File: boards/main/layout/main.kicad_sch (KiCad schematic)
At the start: 150 parts, among them IC1 STM32H725RGV6, IC2 LSM6DSVTR, IC3 TSC2020IYST, IC4 TSC2020IYST, IC5 L6205D013TR, IC6 STSPIN958TR, IC7 L6981N33DR, J1 B02B-PASK(LF)(SN), M1 B02B-PASK(LF)(SN), M2 B02B-PASK(LF)(SN), M3 B02B-PASK(LF)(SN), P1 PZ254V-11-04P, Q1 AO3400A, Q2 AO3400A, Q3 AO3400A, Q4 AO3400A, Q5 AO3400A, Q6 HSBB3072, SW1 DSHP04TJGER, SW2 GT-TC048B-H025-L1, SW3 GT-TC048B-H025-L1, SW4 MK-12D18-G040, SW5 GT-TC048B-H025-L1, U1 TPS611781RNWR, U2 GT-USB-7010ASV, U3 CJA1117B-3.3

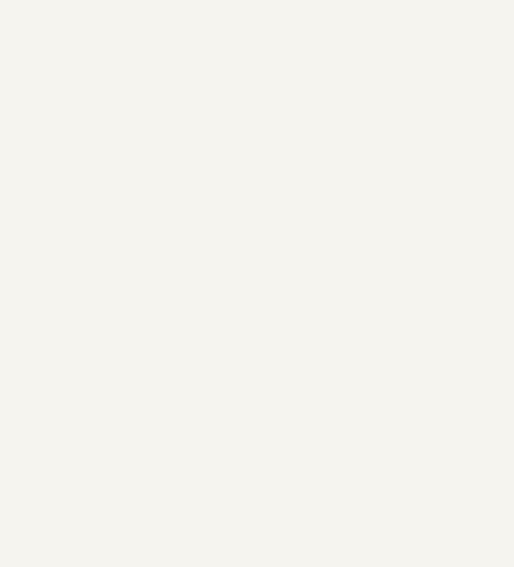
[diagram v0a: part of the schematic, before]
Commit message: ✨ Add the M2 screw holes to the main board
The previous board's four screw holes were footprints without a designator. They are now
H1-H4, instances of a new micras/MountingHole package (2.4 mm NPTH, the previous footprint),
declared in changes.toml as added parts.
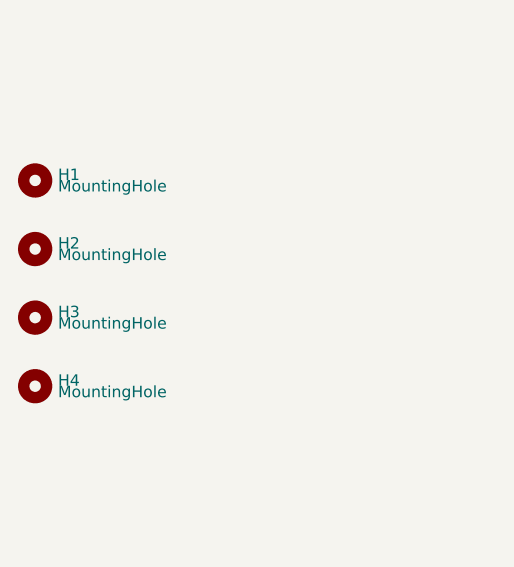
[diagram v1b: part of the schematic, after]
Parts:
- added H1, H2, H3, H4: MountingHole, Team-Micras_MicrasPCB_components_micras_MountingHole:MountingHole_2.4mm_NPTH, symbol MountingHole

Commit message: 🚚 Transfer the Altium pour, teardrop and outline settings to the layouts
The transfer scripts now carry what KiCad's Altium importer drops, and
the layouts are regenerated with them:

- Teardrops (converted to plain zones) fill with a 0.1 mm minimum width
  instead of the importer's 0.25 mm, which left 652 of 786 (main), 5 of
  25 (encoder) and 10 of 46 (bluetooth) teardrops without copper. 0.1 mm
  is JLCPCB's minimum copper feature: 0.0254 mm fills slightly more but
  fails the DFM feature width on all three boards.
- Pours use the Altium polygons' neck width as minimum width (0.1 mm;
  0.4 mm on the encoder's bottom pour, which keeps it out of the channels
  between the SPI tracks, 0.3 mm on the bluetooth plug pour).
- Inner-layer pours relieve through-hole pads (0.254 mm spokes and gap,
  Altium rule PolygonConnect); outer pours stay solid.
- Main In1/In2 keep Altium's 1.559 / 2.074 mm voids around H1-H4
  (copper-pour keepouts).
- Edge.Cuts lines under 1 um (main 6, encoder 1, bluetooth 7) are left
  out and their neighbours joined, so KiCad reads the outlines as valid.
- The board mask expansion is copied from the previous board (0.02 mm);
  main takes the spec's aux origin.
- D4/D5 and bluetooth D1 3D models are scaled to the datasheet heights.
- rework.py catches all six teardrops of the removed C1 VBAT chain (three
  were left as stubs, invisible while unfilled).
- The encoder drops an embedded TSSOP-14 STEP no footprint uses; the
  bluetooth script calls previous.altium_pcb (renamed).

The main layout footprints were resynced from their packages
(pcb layout --sync-footprints), which brings the new WallSensor
silkscreen, R31-R33 and U2's keepouts on all four copper layers.
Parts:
- R31, R32, R33: footprint stdlib_kicad-footprints_Resistor_SMD:R_2512_6332Metric -> Team-Micras_MicrasPCB_components_micras_R2512:RESC6432X89N; symbol R_Small -> R2512
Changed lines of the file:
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@@
 	)
 	(symbol
-		(lib_id "R_Small")
+		(lib_id "R2512")
 		(at 1300.48 736.6 0)
 		(unit 1)
@@
 			)
 		)
-		(property "Footprint" "stdlib_kicad-footprints_Resistor_SMD:R_2512_6332Metric"
+		(property "Footprint" "Team-Micras_MicrasPCB_components_micras_R2512:RESC6432X89N"
 			(at 1300.48 736.6 0)
 			(hide yes)
@@
 	)
 	(symbol
-		(lib_id "R_Small")
+		(lib_id "R2512")
 		(at 1249.68 679.45 0)
 		(unit 1)
@@
 			)
 		)
-		(property "Footprint" "stdlib_kicad-footprints_Resistor_SMD:R_2512_6332Metric"
+		(property "Footprint" "Team-Micras_MicrasPCB_components_micras_R2512:RESC6432X89N"
 			(at 1249.68 679.45 0)
 			(hide yes)
@@
 	)
 	(symbol
-		(lib_id "R_Small")
+		(lib_id "R2512")
 		(at 1270 679.45 0)
 		(unit 1)
@@
 			)
 		)
-		(property "Footprint" "stdlib_kicad-footprints_Resistor_SMD:R_2512_6332Metric"
+		(property "Footprint" "Team-Micras_MicrasPCB_components_micras_R2512:RESC6432X89N"
 			(at 1270 679.45 0)
 			(hide yes)

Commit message: ✨ Give each main-board module its own schematic sheet
Regulators, Drivers, Sensors and Peripherals declare Project(path="layout", layout=False), so pcb apply writes them as sheets of layout/main.kicad_sch (REGULATORS, DRIVERS, SENSORS, PERIPHERALS.kicad_sch) and the layout stays the board's: main.kicad_pcb is byte-identical.

make gen deletes every .kicad_sch of a layout before pcb apply: pcb refuses to write a new root over existing module sheets, and a regenerated sheet must not keep labels from an older generator.

ERC fails on the sheets until the ports take their nets' names (next commit) and the warnings pcb 0.4.81 leaves on module sheets are accepted (diodeinc/pcb#1520).
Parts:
- removed BZ1: FUET-5030, Team-Micras_MicrasPCB_components_fuet_FUET-5030:BUZ-SMD_FST-5030, symbol FUET-5030
- removed C18, C19, C20, C21, C24, C25, C32, C38, C55, C60: 100nF 10% 50V X7R, stdlib_kicad-footprints_Capacitor_SMD:C_0402_1005Metric, symbol C_Small
- removed C22, C23: 18pF 5% 50V C0G, stdlib_kicad-footprints_Capacitor_SMD:C_0402_1005Metric, symbol C_Small
- removed C26, C27, C28, C29, C33, C53, C54: 1uF 10% 25V X5R, stdlib_kicad-footprints_Capacitor_SMD:C_0402_1005Metric, symbol C_Small
- removed C30, C40, C41: 10nF 10% 50V X7R, stdlib_kicad-footprints_Capacitor_SMD:C_0402_1005Metric, symbol C_Small
- removed C31: 220nF 10% 16V X7R, stdlib_kicad-footprints_Capacitor_SMD:C_0402_1005Metric, symbol C_Small
- removed C34, C35: 470nF 10% 25V X7R, stdlib_kicad-footprints_Capacitor_SMD:C_0603_1608Metric, symbol C_Small
- removed C36: 220uF 20% 16V, Team-Micras_MicrasPCB_components_acmecon_VT1C221M0605:CAP-SMD_BD6.3-L6.6-W6.6-LS7.3-FD, symbol VT1C221M0605
- removed C37: 100uF 20% 25V, Team-Micras_MicrasPCB_components_jierr_JVS25V100M6X4:CAP-SMD_BD6.3-L6.6-W6.6-LS7.3-FD_JVS25V100M6X4, symbol JVS25V100M6X4
- removed C39: 220nF 10% 50V X7R, stdlib_kicad-footprints_Capacitor_SMD:C_0805_2012Metric, symbol C_Small
- removed C42: 470pF 10% 50V X7R, stdlib_kicad-footprints_Capacitor_SMD:C_0402_1005Metric, symbol C_Small
- removed C43: 220nF 10% 25V X7R, stdlib_kicad-footprints_Capacitor_SMD:C_0603_1608Metric, symbol C_Small
- removed C44, C45: 10uF 10% 50V X5R, stdlib_kicad-footprints_Capacitor_SMD:C_0805_2012Metric, symbol C_Small
- removed C46, C47: 22uF 20% 35V X5R, stdlib_kicad-footprints_Capacitor_SMD:C_0805_2012Metric, symbol C_Small
- removed C48: 4.7uF 10% 25V X5R, stdlib_kicad-footprints_Capacitor_SMD:C_0805_2012Metric, symbol C_Small
- removed C49, C50, C51, C57: 22uF 20% 25V X5R, stdlib_kicad-footprints_Capacitor_SMD:C_0805_2012Metric, symbol C_Small
- removed C52: 10uF 20% 25V X5R, stdlib_kicad-footprints_Capacitor_SMD:C_0603_1608Metric, symbol C_Small
- removed C56: 220uF 20% 6.3V X5R, stdlib_kicad-footprints_Capacitor_SMD:C_1206_3216Metric, symbol C_Small
- removed D1, D2: WS2815C-2020-4P, Team-Micras_MicrasPCB_components_worldsemi_WS2815C-2020:LED-SMD_4P-L2.2-W2.0-P1.00_WS2815C-2020-4P, symbol WS2815C-2020-4P
- removed D3, D6, D7: 1N4148W, Team-Micras_MicrasPCB_components_hongjiacheng_1N4148W:SOD-123_L2.7-W1.6-LS3.7-FD, symbol 1N4148W
- removed D4: LED YELLOW, stdlib_kicad-footprints_LED_SMD:LED_0603_1608Metric, symbol LED_Small_Filled_Yellow
- removed D5: LED RED, stdlib_kicad-footprints_LED_SMD:LED_0603_1608Metric, symbol LED_Small_Filled_Red
- removed EC1, EC2: EncoderSlot, Team-Micras_MicrasPCB_components_micras_EncoderSlot:EncoderSlot_2x4_P0.95mm, symbol EncoderSlot
- removed F1: KASML010, Team-Micras_MicrasPCB_components_kuu_KASML010:Fuse_0402, symbol KASML010
- removed IC2: LSM6DSVTR, Team-Micras_MicrasPCB_components_st_LSM6DSV:LGA-14_3x2.5mm_P0.5mm, symbol LSM6DSV
- removed IC3, IC4: TSC2020IYST, Team-Micras_MicrasPCB_components_st_TSC2020:SOP65P490X110-8N, symbol TSC2020
- removed IC5: L6205D013TR, Team-Micras_MicrasPCB_components_st_L6205D:SOIC127P1032X265-20N, symbol L6205D
- removed IC6: STSPIN958TR, Team-Micras_MicrasPCB_components_st_STSPIN958:QFN50P500X500X100-33N-D, symbol STSPIN958
- removed IC7: L6981N33DR, Team-Micras_MicrasPCB_components_st_L6981:SOIC127P600X175-8N, symbol L6981N33DR
- removed J1, M1, M2, M3: B02B-PASK(LF)(SN), Team-Micras_MicrasPCB_components_jst_B02B-PASK:JST_PA_B02B-PASK_1x02_P2.00mm_Vertical, symbol B02B-PASK
- removed L2: 1uH 20% 23A, Team-Micras_MicrasPCB_components_coilcraft_XAL6030-102:XAL6030, symbol XAL6030-102MEB
- removed L3: 22uH 20% 2.8A, Team-Micras_MicrasPCB_components_yjycoin_YSPIA0645-220M:IND-SMD_L6.5-W6.0, symbol YSPIA0645-220M
- removed Q1, Q2, Q3, Q4, Q5: AO3400A, Team-Micras_MicrasPCB_components_aos_AO3400A:SOT-23-3_L2.9-W1.3-P1.90-LS2.4-BR, symbol AO3400A
- removed Q6: HSBB3072, Team-Micras_MicrasPCB_components_huashuo_HSBB3072:PRPAK-8_L3.0-W3.0-P0.65-BL-EP, symbol HSBB3072
- removed R1, R11, R15, R19, R23: 220 1%, stdlib_kicad-footprints_Resistor_SMD:R_0402_1005Metric, symbol R_Small
- removed R10: 1.5k 1%, stdlib_kicad-footprints_Resistor_SMD:R_0402_1005Metric, symbol R_Small
- removed R12, R16, R2, R20, R24, R42: 10k 1%, stdlib_kicad-footprints_Resistor_SMD:R_0402_1005Metric, symbol R_Small
- removed R13, R17, R21, R25, R3: 10 1% 100mW, stdlib_kicad-footprints_Resistor_SMD:R_0603_1608Metric, symbol R_Small
- removed R14, R18, R22, R26: 1k 1%, stdlib_kicad-footprints_Resistor_SMD:R_0402_1005Metric, symbol R_Small
- removed R27: 39k 1%, stdlib_kicad-footprints_Resistor_SMD:R_0402_1005Metric, symbol R_Small
- removed R28: 24k 1%, stdlib_kicad-footprints_Resistor_SMD:R_0402_1005Metric, symbol R_Small
- removed R29: 75k 1%, stdlib_kicad-footprints_Resistor_SMD:R_0402_1005Metric, symbol R_Small
- removed R30: 5.6k 1%, stdlib_kicad-footprints_Resistor_SMD:R_0402_1005Metric, symbol R_Small
- removed R31: 50m 1% 3W, Team-Micras_MicrasPCB_components_micras_R2512:RESC6432X89N, symbol R2512
- removed R32, R33: 40m 1% 2W, Team-Micras_MicrasPCB_components_micras_R2512:RESC6432X89N, symbol R2512
- removed R34: 100 1%, stdlib_kicad-footprints_Resistor_SMD:R_0402_1005Metric, symbol R_Small
- removed R35, R41: 100k 1%, stdlib_kicad-footprints_Resistor_SMD:R_0402_1005Metric, symbol R_Small
- removed R36: 150k 1%, stdlib_kicad-footprints_Resistor_SMD:R_0402_1005Metric, symbol R_Small
- removed R37: 56k 1%, stdlib_kicad-footprints_Resistor_SMD:R_0402_1005Metric, symbol R_Small
- removed R38: 68k 1%, stdlib_kicad-footprints_Resistor_SMD:R_0402_1005Metric, symbol R_Small
- removed R39: 2M 1% 100mW, stdlib_kicad-footprints_Resistor_SMD:R_0603_1608Metric, symbol R_Small
- removed R4, R5: 680 1%, stdlib_kicad-footprints_Resistor_SMD:R_0402_1005Metric, symbol R_Small
- removed R40: 130k 1% 100mW, stdlib_kicad-footprints_Resistor_SMD:R_0603_1608Metric, symbol R_Small
- removed R6, R7: 5.1k 1%, stdlib_kicad-footprints_Resistor_SMD:R_0402_1005Metric, symbol R_Small
- removed R8, R9: 33 1%, stdlib_kicad-footprints_Resistor_SMD:R_0402_1005Metric, symbol R_Small
- removed SW1: DSHP04TJGER, Team-Micras_MicrasPCB_components_kangshen_DSHP04TJGER:SW-SMD_8P-L6.7-W5.4-P1.27-LS5.6, symbol DSHP04TJGER
- removed SW2, SW3, SW5: GT-TC048B-H025-L1, Team-Micras_MicrasPCB_components_g-switch_GT-TC048B-H025-L1:SW-SMD-4P_L4.2-W3.2_GT-TC048, symbol GT-TC048B-H025-L1
- removed SW4: MK-12D18-G040, Team-Micras_MicrasPCB_components_g-switch_MK-12D18-G040:SW-TH_MK-12D18-G040, symbol MK-12D18-G040
- removed U1: TPS611781RNWR, Team-Micras_MicrasPCB_components_ti_TPS61178:RNW0013A, symbol TPS611781RNWR
- removed U2: GT-USB-7010ASV, Team-Micras_MicrasPCB_components_g-switch_GT-USB-7010ASV:USB-C_G-Switch_GT-USB-7010ASV, symbol GT-USB-7010ASV
- removed U3: CJA1117B-3.3, Team-Micras_MicrasPCB_components_cj_CJA1117B:SOT-89-3_L4.5-W2.5-P1.50-LS4.2-BR, symbol CJA1117B-3.3
- removed W1, W2, W3, W4: WallSensor, Team-Micras_MicrasPCB_components_micras_WallSensor:WallSensor_SFH4550_TPS601A_THT, symbol WallSensor
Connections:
- no-connect marks 15 -> 5
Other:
- added sheet DRIVERS (DRIVERS.kicad_sch)
- added sheet PERIPHERALS (PERIPHERALS.kicad_sch)
- added sheet REGULATORS (REGULATORS.kicad_sch)
- added sheet SENSORS (SENSORS.kicad_sch)
- moved on the sheet: 20V1, C1, C10, C11, C12, C13, C14, C15, C16, C17, C2, C3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

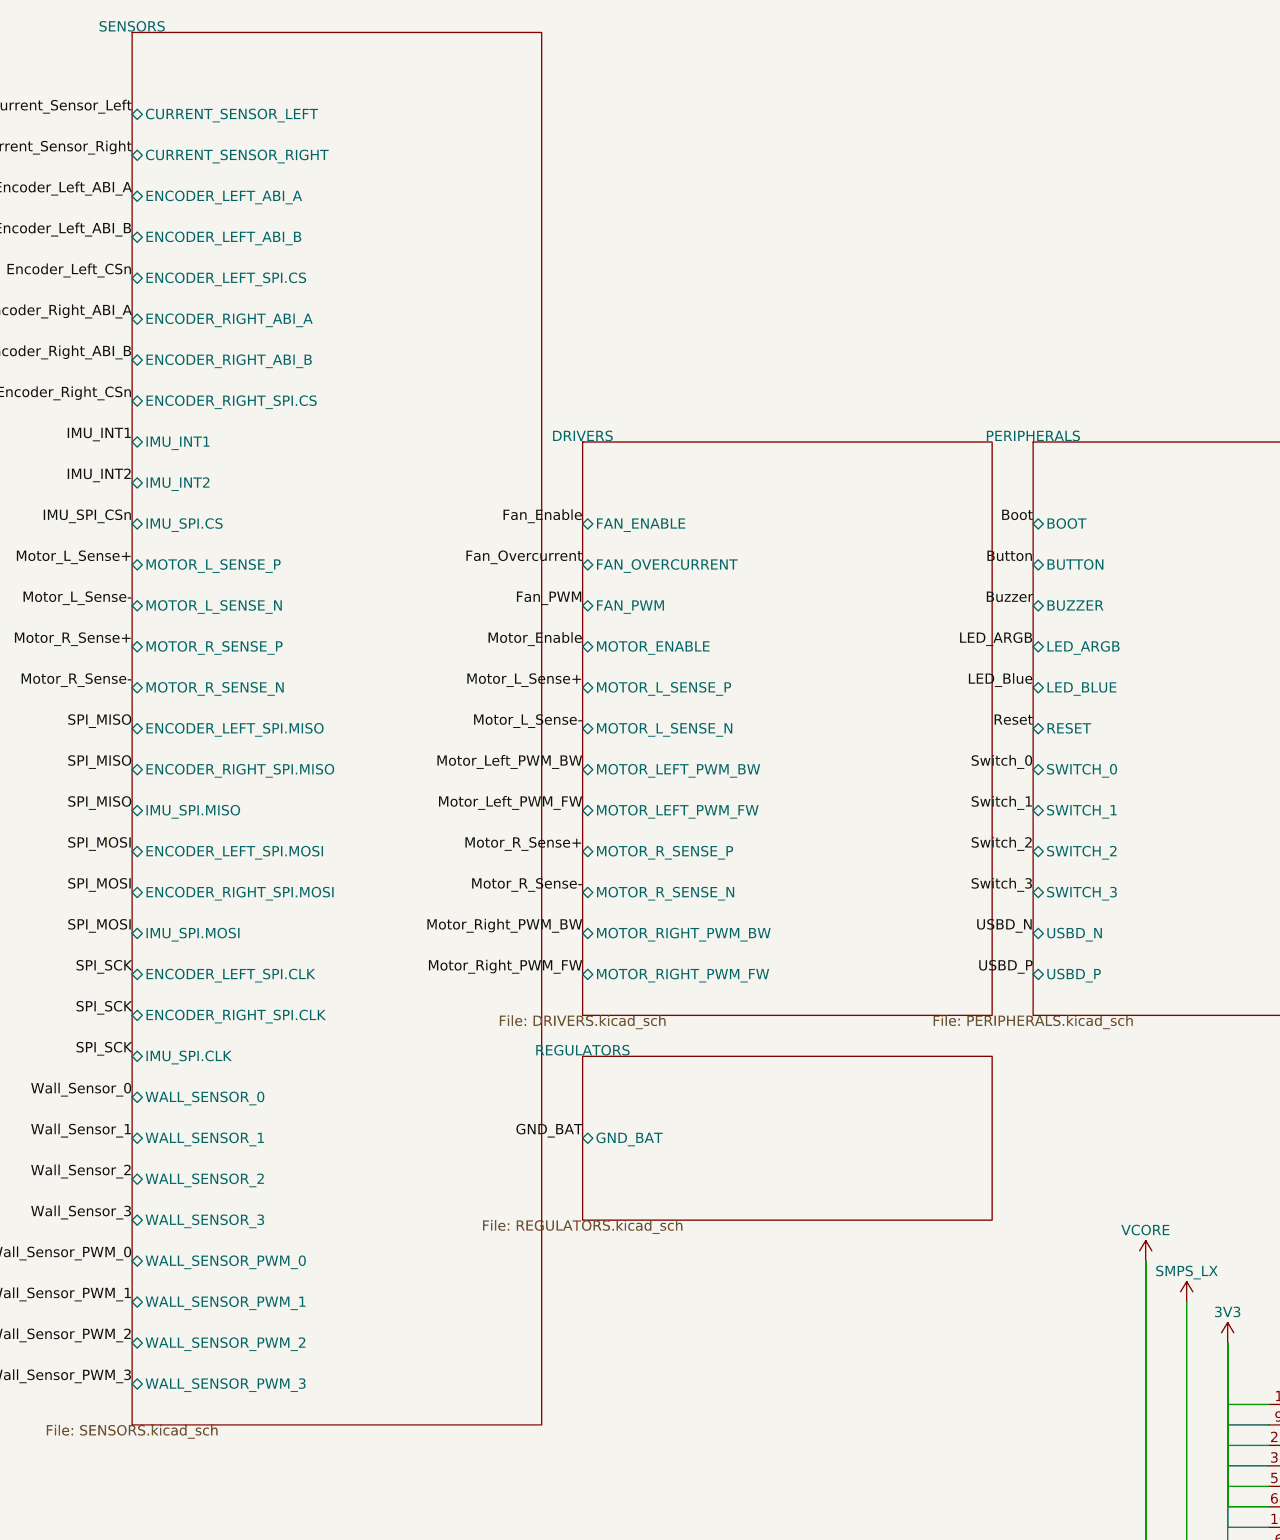
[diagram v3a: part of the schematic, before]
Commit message: 🏷️ Name the main board's module ports after their nets
A module's signal port now takes the name of the board net it carries (Fan_Enable, Wall_Sensor_0, Button), so its sheet pin and hierarchical label match the root's label: KiCad's ERC flagged each pair as similar_labels, names that differ only in case. The SPI buses and the Motor_*_Sense+/- nets, whose names are not identifiers, keep their port names. GND_BAT becomes a ground port of REGULATORS, so it reaches the root as a power symbol at the sheet pin instead of a dangling label. The netlist is unchanged: same nets, same names.
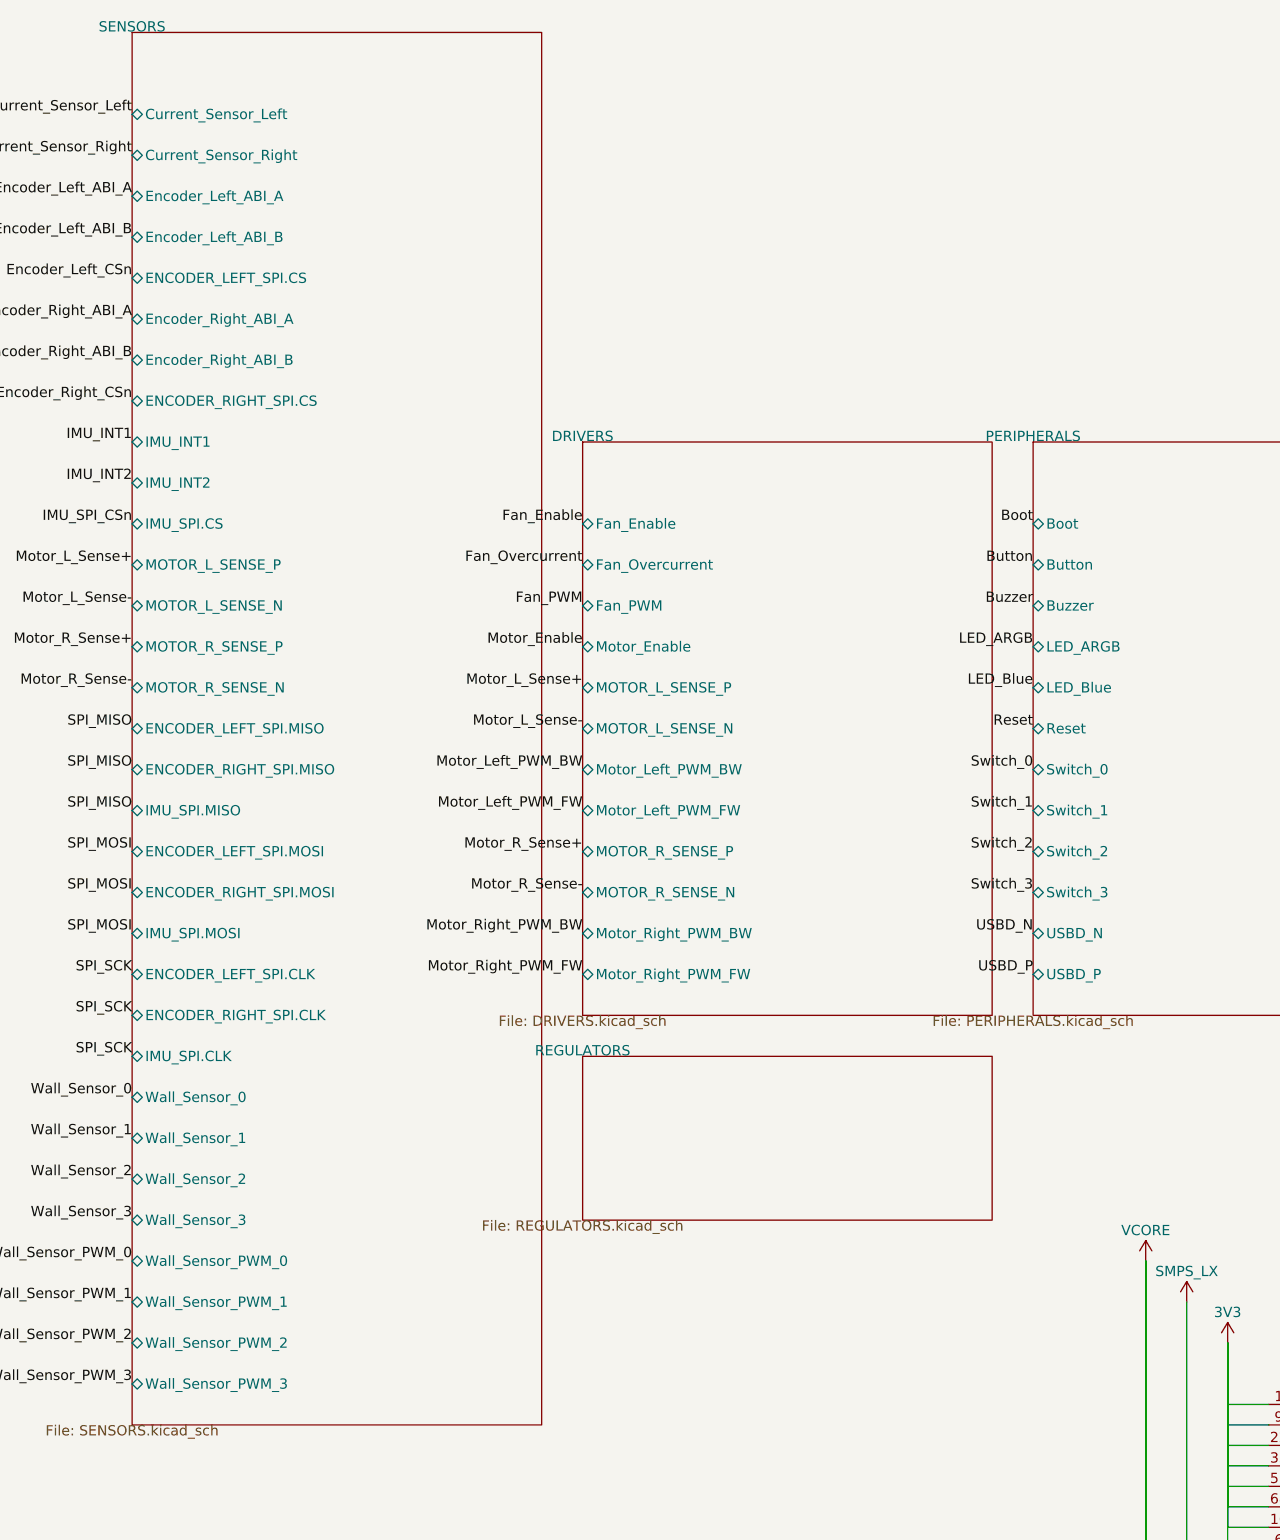
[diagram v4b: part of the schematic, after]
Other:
- sheet DRIVERS ports: added Fan_Enable, Fan_Overcurrent, Fan_PWM, Motor_Enable, Motor_Left_PWM_BW, Motor_Left_PWM_FW, Motor_Right_PWM_BW, Motor_Right_PWM_FW; removed FAN_ENABLE, FAN_OVERCURRENT, FAN_PWM, MOTOR_ENABLE, MOTOR_LEFT_PWM_BW, MOTOR_LEFT_PWM_FW, MOTOR_RIGHT_PWM_BW, MOTOR_RIGHT_PWM_FW
- sheet PERIPHERALS ports: added Boot, Button, Buzzer, LED_Blue, Reset, Switch_0, Switch_1, Switch_2, Switch_3; removed BOOT, BUTTON, BUZZER, LED_BLUE, RESET, SWITCH_0, SWITCH_1, SWITCH_2, SWITCH_3
- sheet REGULATORS ports: added none; removed GND_BAT
- sheet SENSORS ports: added Current_Sensor_Left, Current_Sensor_Right, Encoder_Left_ABI_A, Encoder_Left_ABI_B, Encoder_Right_ABI_A, Encoder_Right_ABI_B, Wall_Sensor_0, Wall_Sensor_1, Wall_Sensor_2, Wall_Sensor_3, Wall_Sensor_PWM_0, Wall_Sensor_PWM_1, Wall_Sensor_PWM_2, Wall_Sensor_PWM_3; removed CURRENT_SENSOR_LEFT, CURRENT_SENSOR_RIGHT, ENCODER_LEFT_ABI_A, ENCODER_LEFT_ABI_B, ENCODER_RIGHT_ABI_A, ENCODER_RIGHT_ABI_B, WALL_SENSOR_0, WALL_SENSOR_1, WALL_SENSOR_2, WALL_SENSOR_3, WALL_SENSOR_PWM_0, WALL_SENSOR_PWM_1, WALL_SENSOR_PWM_2, WALL_SENSOR_PWM_3

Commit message: 🎨 Place this revision's root, REGULATORS and SENSORS sheets; give the CJA1117B room for its pin names
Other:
- note added: "- No HSE or LSE crystal: PC15 and PH1 are unused."
- note added: "- VDD, VDDSMPS and VBAT on 3V3 (no backup battery)."
- note added: "- VDDA is also VREF+ on this package: on 3V3, with"
- note added: "- VLXSMPS drives L1; VFBSMPS and VCAP1-3 all on VCORE."
- note added: "100 nF per VDD pin"
- note added: "C10 and C11 at the pin."
- note added: "C8, C9 at VBAT; C17 bulk"
- note added: "Direct SMPS supply (DS13311; AN5419 Table 2, Figure 5):"
- note added: "MCU: STM32H725RGV6, Direct SMPS supply and decoupling"
- note added: "Module sheets"
- note added: "Mounting holes (M2)"
- note added: "SWD debug connector"
- note added: "Test points (bare pads)"
- note added: "The firmware selects PWR_DIRECT_SMPS_SUPPLY."
- note added: "VCORE from the SMPS: 2 x 10 uF at L1, 100 nF per VCAP"
- note added: "VDDA (= VREF+): 1 uF + 100 nF at the pin"
- note added: "VDDSMPS: 10 uF + 4.7 uF"
- title: (none) -> MCU, debug and module sheets
- moved on the sheet: 20V1, C1, C10, C11, C12, C13, C14, C15, C16, C17, C2, C3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
